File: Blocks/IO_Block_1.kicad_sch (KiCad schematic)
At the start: 12 parts, among them IC1 TLP172AM_TPR,E, IC2 TLP172AM_TPR,E, IC3 TLP172AM_TPR,E, IC4 TLP172AM_TPR,E, IC5 TLP172AM_TPR,E, IC6 TLP172AM_TPR,E

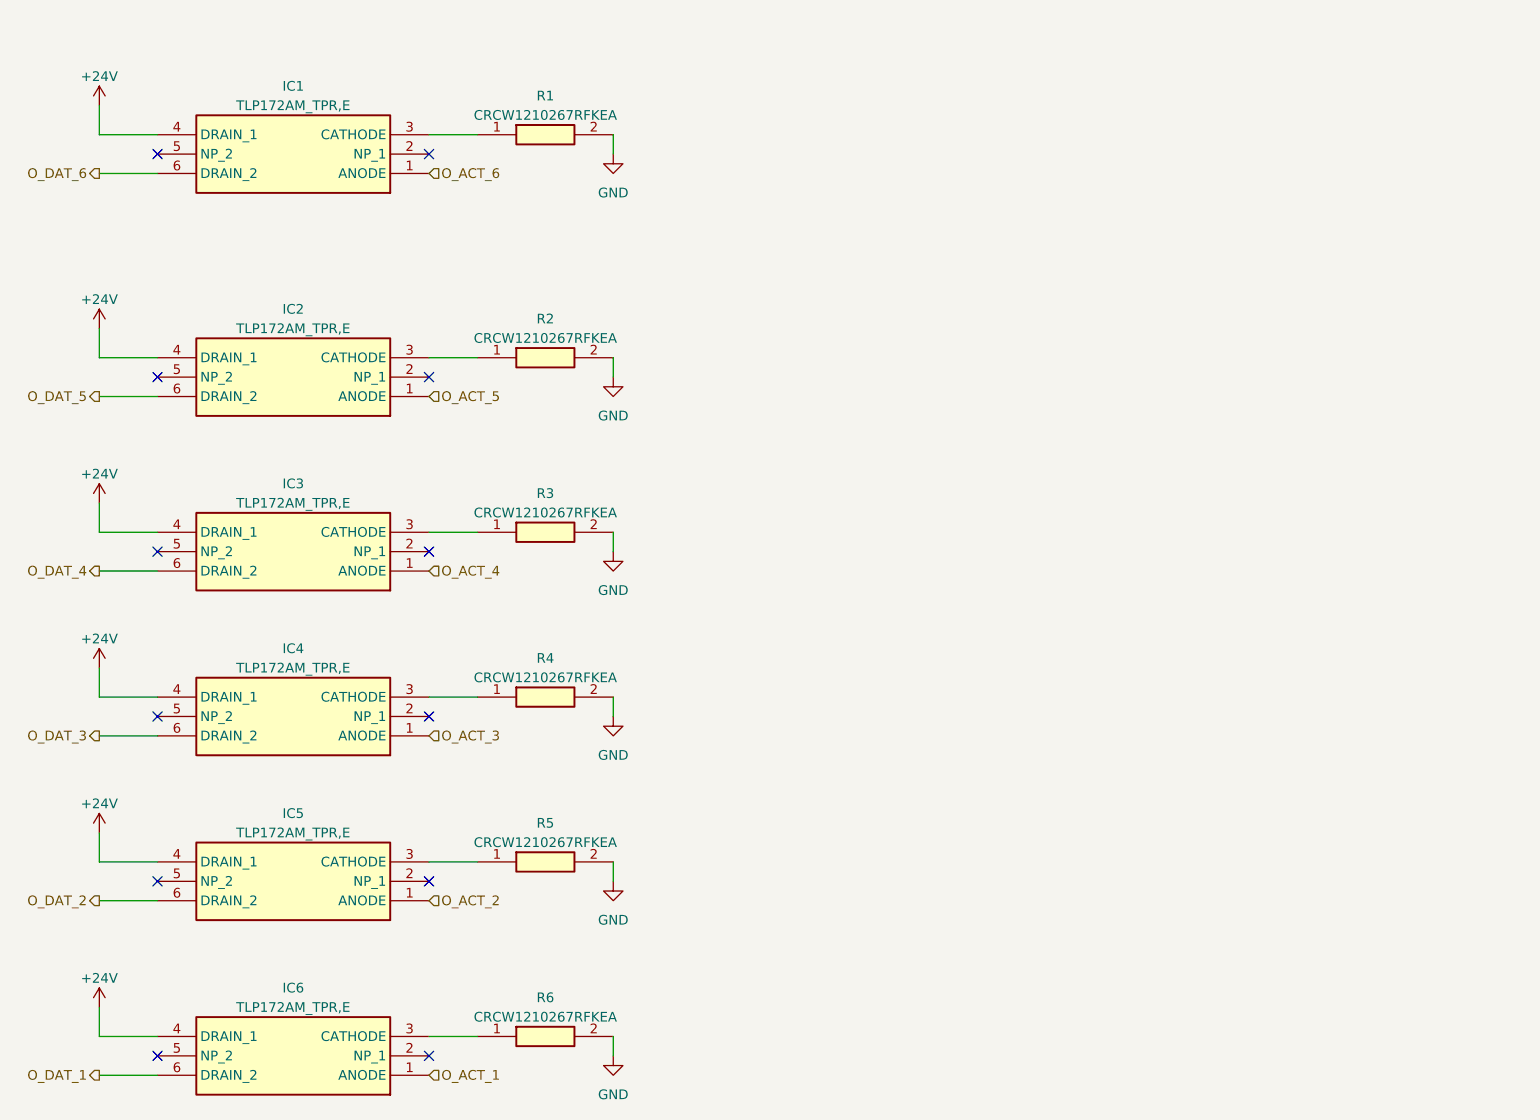
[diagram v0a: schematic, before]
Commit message: Automate library addition * Added script to automagically extract samacsys libraries and put them in corresponding folders. * Note: Requires zsh
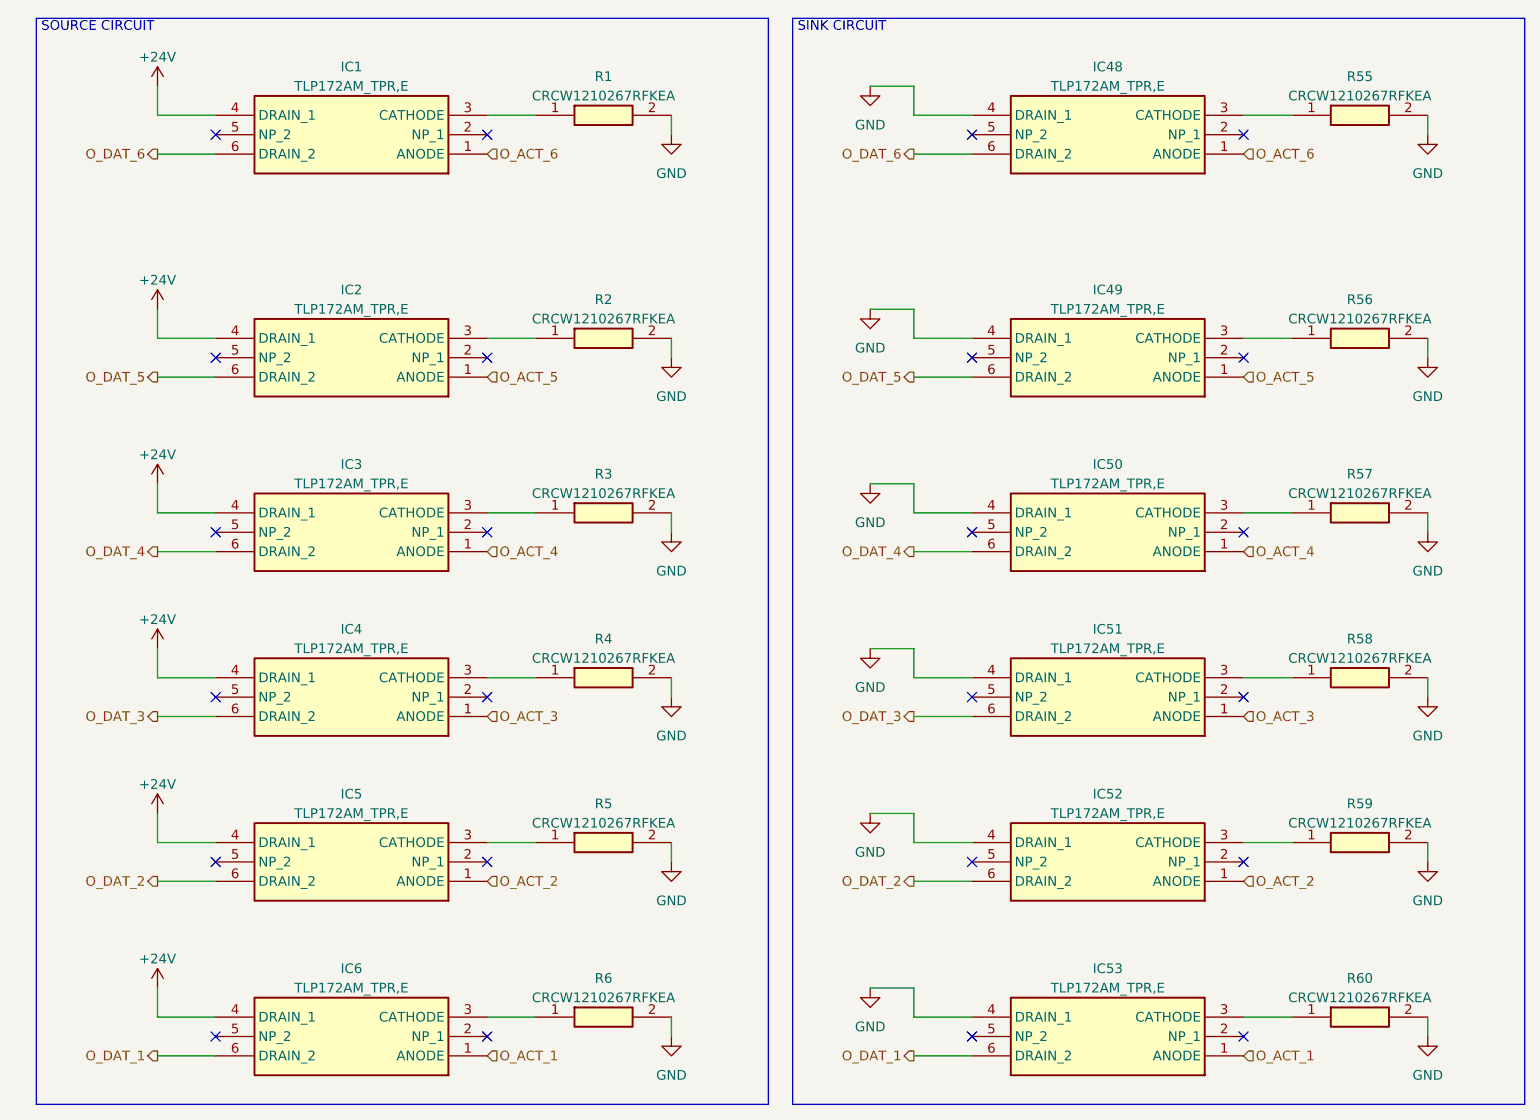
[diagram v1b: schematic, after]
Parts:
- added IC48, IC49, IC50, IC51, IC52, IC53: TLP172AM_TPR,E, TLP172AM_TPR_E:SOIC127P700X230-6N, symbol TLP172AM_TPR_E:TLP172AM_TPR,E
- added R55, R56, R57, R58, R59, R60: CRCW1210267RFKEA, CRCW1210267RFKEA:RESC3225X60N, symbol CRCW1210267RFKEA:CRCW1210267RFKEA
- IC1, IC2, IC3, IC4, IC5, IC6: footprint LIB_TLP172AM_TPR,E:SOIC127P700X230-6N -> TLP172AM_TPR_E:SOIC127P700X230-6N
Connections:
- net GND: now also IC48.4 (DRAIN_1), IC49.4 (DRAIN_1), IC50.4 (DRAIN_1), IC51.4 (DRAIN_1), IC52.4 (DRAIN_1), IC53.4 (DRAIN_1), R55.2, R56.2, R57.2, R58.2, R59.2, R60.2
- net O_ACT_1: now also IC53.1 (ANODE)
- net O_ACT_2: now also IC52.1 (ANODE)
- net O_ACT_3: now also IC51.1 (ANODE)
- net O_ACT_4: now also IC50.1 (ANODE)
- net O_ACT_5: now also IC49.1 (ANODE)
- net O_ACT_6: now also IC48.1 (ANODE)
- net O_DAT_1: now also IC53.6 (DRAIN_2)
- net O_DAT_2: now also IC52.6 (DRAIN_2)
- net O_DAT_3: now also IC51.6 (DRAIN_2)
- net O_DAT_4: now also IC50.6 (DRAIN_2)
- net O_DAT_5: now also IC49.6 (DRAIN_2)
- net O_DAT_6: now also IC48.6 (DRAIN_2)
- new net: IC53.3 (CATHODE), R60.1
- new net: IC51.3 (CATHODE), R58.1
- new net: IC49.3 (CATHODE), R56.1
- new net: IC50.3 (CATHODE), R57.1
- new net: IC48.3 (CATHODE), R55.1
- new net: IC52.3 (CATHODE), R59.1
- no-connect marks 12 -> 24
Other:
- note added: "SINK CIRCUIT"
- note added: "SOURCE CIRCUIT"
- moved on the sheet: IC1, IC2, IC3, IC4, IC5, IC6, R1, R2, R3, R4, R5, R6
